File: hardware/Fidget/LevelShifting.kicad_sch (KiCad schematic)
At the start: 18 parts

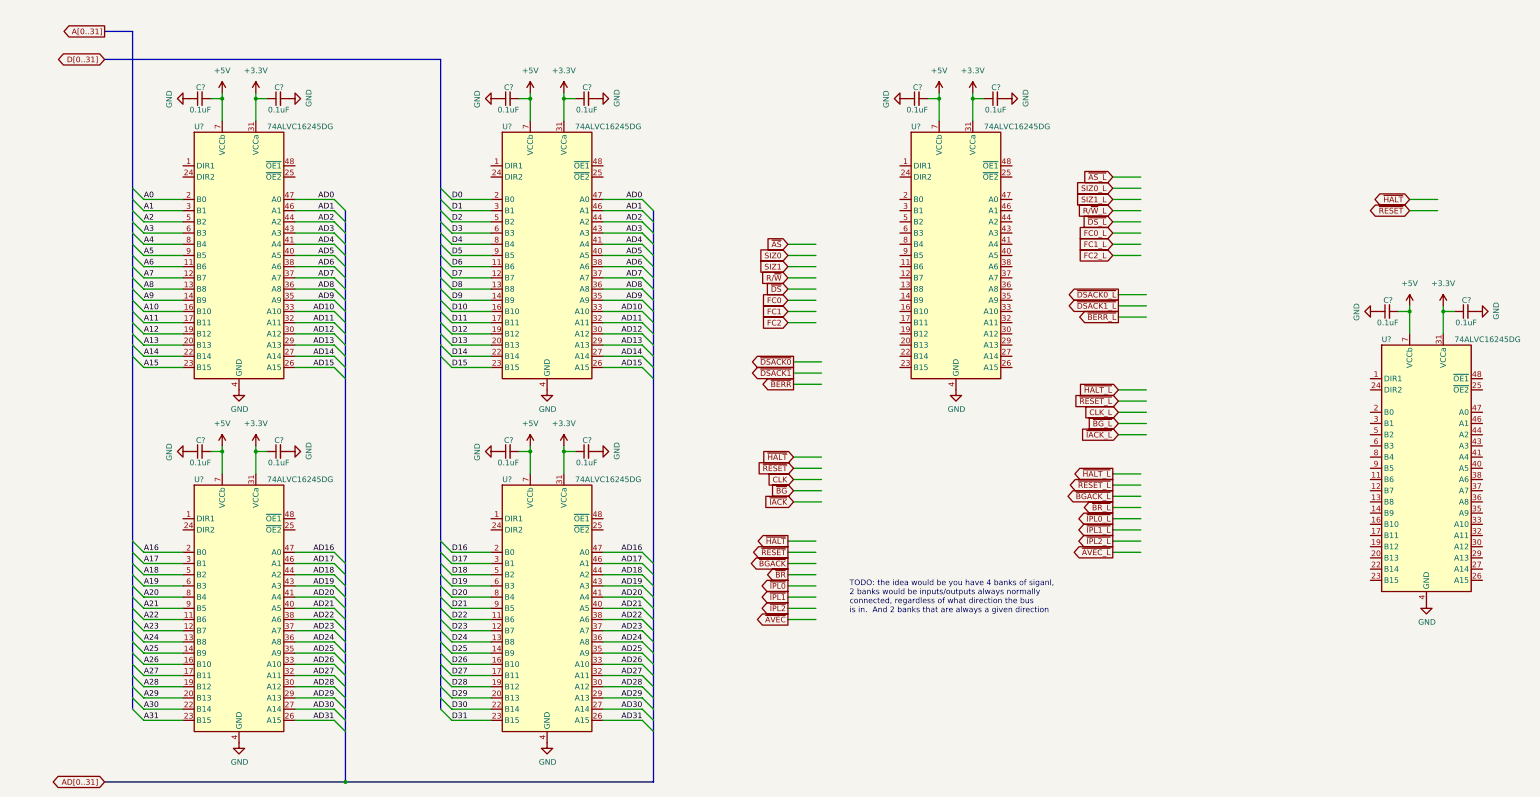
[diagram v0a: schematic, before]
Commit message: Assigned bus control signals to level shifters
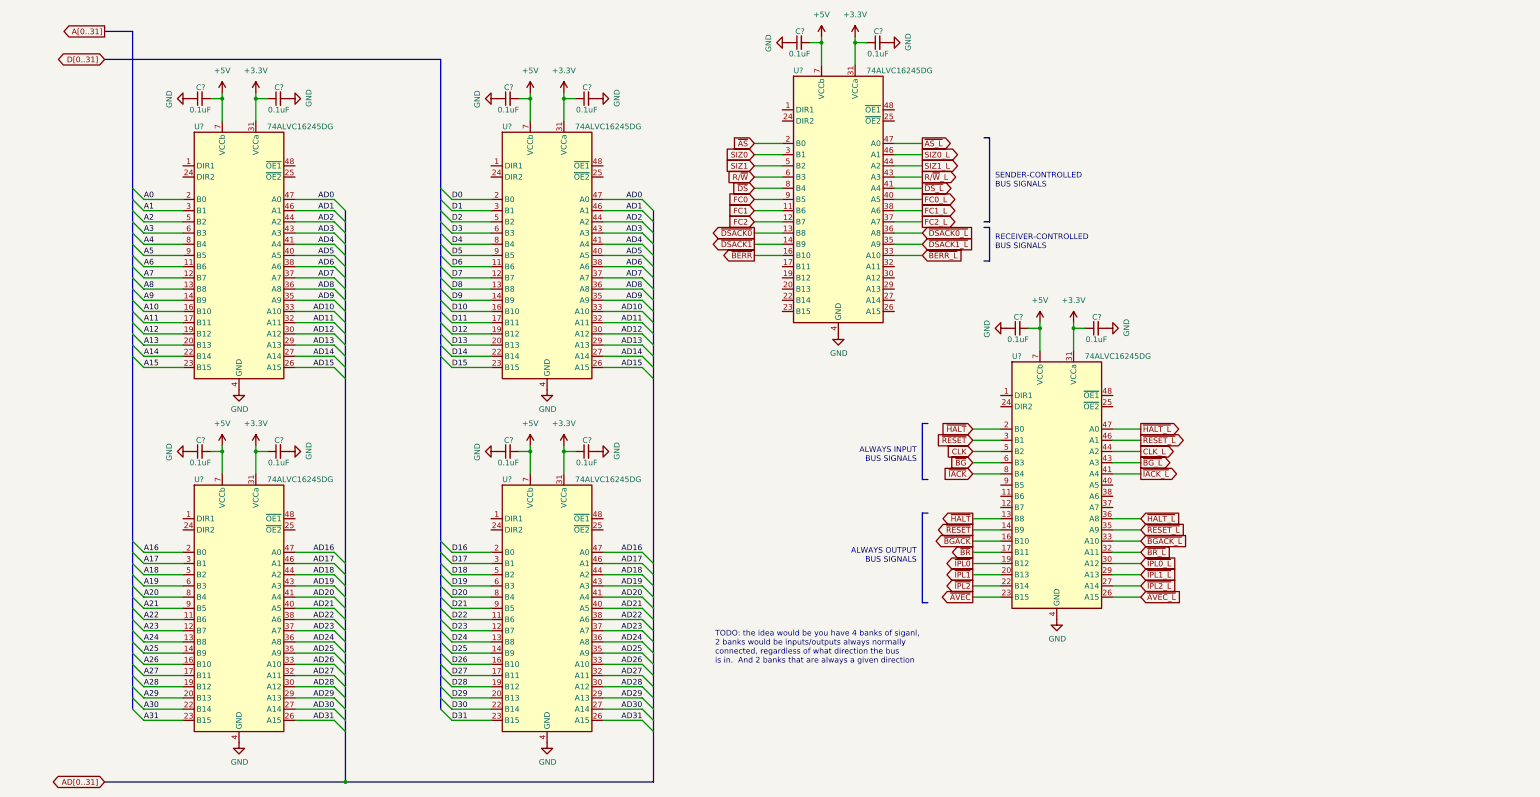
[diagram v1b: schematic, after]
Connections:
- net CLK: now also U?.5 (B2)
- net CLK_L: now also U?.44 (A2)
- net FC0: now also U?.9 (B5)
- net FC0_L: now also U?.40 (A5)
- net FC1: now also U?.11 (B6)
- net FC1_L: now also U?.38 (A6)
- net FC2: now also U?.12 (B7)
- net FC2_L: now also U?.37 (A7)
- net R/~{W}: now also U?.6 (B3)
- net R/~{W}_L: now also U?.43 (A3)
- net SIZ0: now also U?.3 (B1)
- net SIZ0_L: now also U?.46 (A1)
- net SIZ1: now also U?.5 (B2)
- net SIZ1_L: now also U?.44 (A2)
- net ~{AS_L}: now also U?.47 (A0)
- net ~{AS}: now also U?.2 (B0)
- net ~{AVEC_L}: now also U?.26 (A15)
- net ~{AVEC}: now also U?.23 (B15)
- net ~{BERR_L}: now also U?.33 (A10)
- net ~{BERR}: now also U?.16 (B10)
- net ~{BGACK_L}: now also U?.33 (A10)
- net ~{BGACK}: now also U?.16 (B10)
- net ~{BG_L}: now also U?.43 (A3)
- net ~{BG}: now also U?.6 (B3)
- net ~{BR_L}: now also U?.32 (A11)
- net ~{BR}: now also U?.17 (B11)
- net ~{DSACK0_L}: now also U?.36 (A8)
- net ~{DSACK0}: now also U?.13 (B8)
- net ~{DSACK1_L}: now also U?.35 (A9)
- net ~{DSACK1}: now also U?.14 (B9)
- net ~{DS_L}: now also U?.41 (A4)
- net ~{DS}: now also U?.8 (B4)
- net ~{HALT_L}: now also U?.36 (A8), U?.47 (A0)
- net ~{HALT}: now also U?.13 (B8), U?.2 (B0)
- net ~{IACK_L}: now also U?.41 (A4)
- net ~{IACK}: now also U?.8 (B4)
- net ~{IPL0_L}: now also U?.30 (A12)
- net ~{IPL0}: now also U?.19 (B12)
- net ~{IPL1_L}: now also U?.29 (A13)
- net ~{IPL1}: now also U?.20 (B13)
- net ~{IPL2_L}: now also U?.27 (A14)
- net ~{IPL2}: now also U?.22 (B14)
- net ~{RESET_L}: now also U?.35 (A9), U?.46 (A1)
- net ~{RESET}: now also U?.14 (B9), U?.3 (B1)
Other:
- note added: "ALWAYS INPUT BUS SIGNALS"
- note added: "ALWAYS OUTPUT BUS SIGNALS"
- note added: "RECEIVER-CONTROLLED BUS SIGNALS"
- note added: "SENDER-CONTROLLED BUS SIGNALS"
- moved on the sheet: C?, U?

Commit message: Added address latches
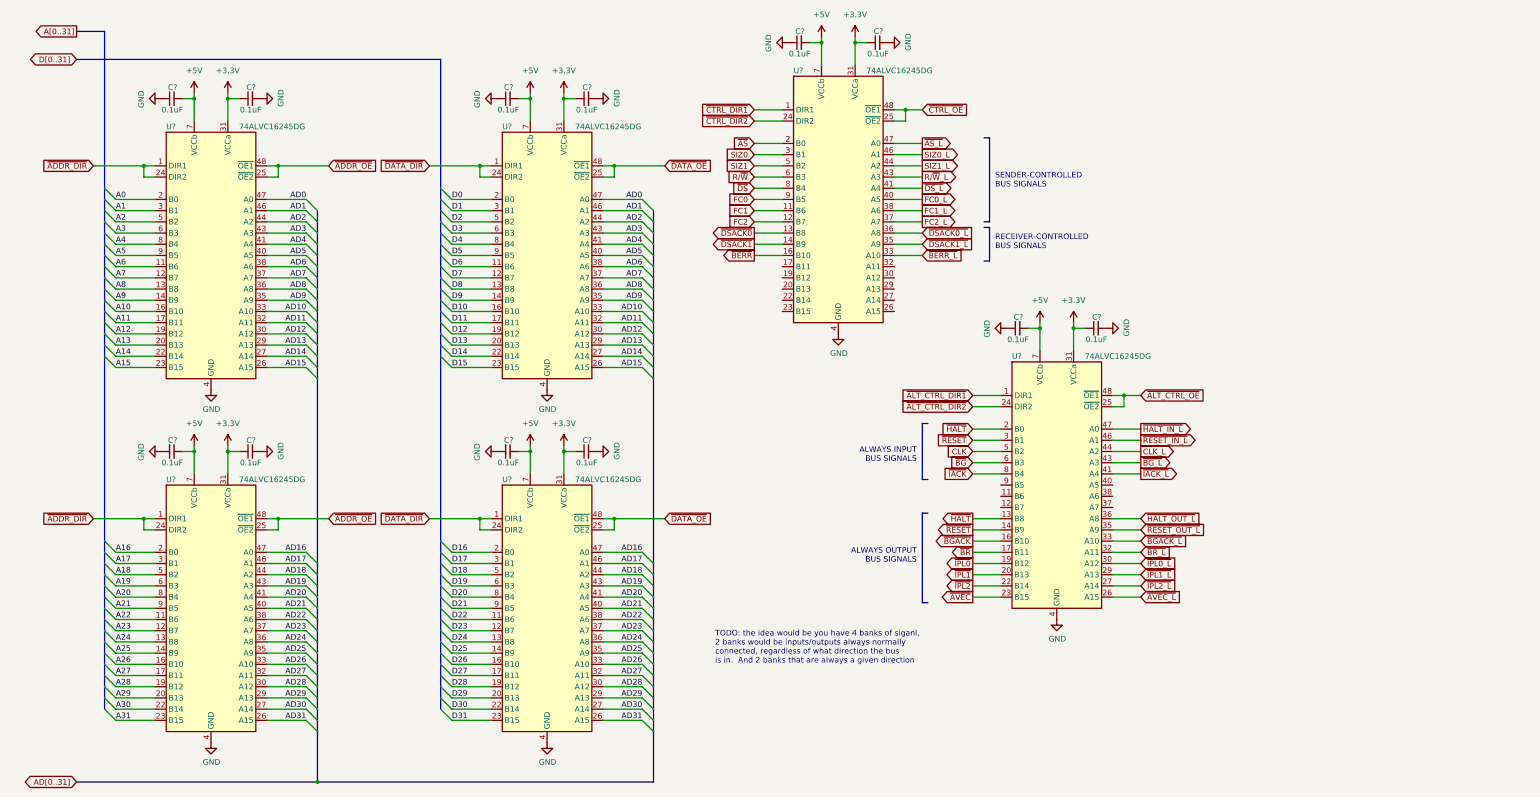
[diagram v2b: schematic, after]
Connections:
- net ~{DATA_DIR}: now reaches U?.1 (DIR1)
- net ~{DATA_DIR}: now also U?.1 (DIR1), U?.24 (DIR2), U?.24 (DIR2)
- net ~{DATA_OE}: now reaches U?.25 (~{OE2})
- net ~{DATA_OE}: now also U?.25 (~{OE2}), U?.48 (~{OE1}), U?.48 (~{OE1})
- net ~{ADDR_DIR}: now reaches U?.1 (DIR1)
- net ~{ADDR_DIR}: now also U?.1 (DIR1), U?.24 (DIR2), U?.24 (DIR2)
- net ~{ADDR_OE}: now reaches U?.25 (~{OE2})
- net ~{ADDR_OE}: now also U?.25 (~{OE2}), U?.48 (~{OE1}), U?.48 (~{OE1})
- net ~{CTRL_DIR1}: now reaches U?.1 (DIR1)
- net ~{CTRL_DIR2}: now reaches U?.24 (DIR2)
- net ~{CTRL_OE}: now reaches U?.25 (~{OE2})
- net ~{CTRL_OE}: now also U?.48 (~{OE1})
- net ~{ALT_CTRL_DIR1}: now reaches U?.1 (DIR1)
- net ~{ALT_CTRL_DIR2}: now reaches U?.24 (DIR2)
- net ~{ALT_CTRL_OE}: now reaches U?.25 (~{OE2})
- net ~{ALT_CTRL_OE}: now also U?.48 (~{OE1})
- net ~{HALT_L} renamed ~{HALT_IN_L}
- net ~{HALT_IN_L}: no longer U?.36 (A8)
- net ~{RESET_L} renamed ~{RESET_IN_L}
- net ~{RESET_IN_L}: no longer U?.35 (A9)
- new net ~{HALT_OUT_L}: U?.36 (A8)
- new net ~{RESET_OUT_L}: U?.35 (A9)
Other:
- moved on the sheet: C?, U?

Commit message: Progress on sorting out the transceiver controls
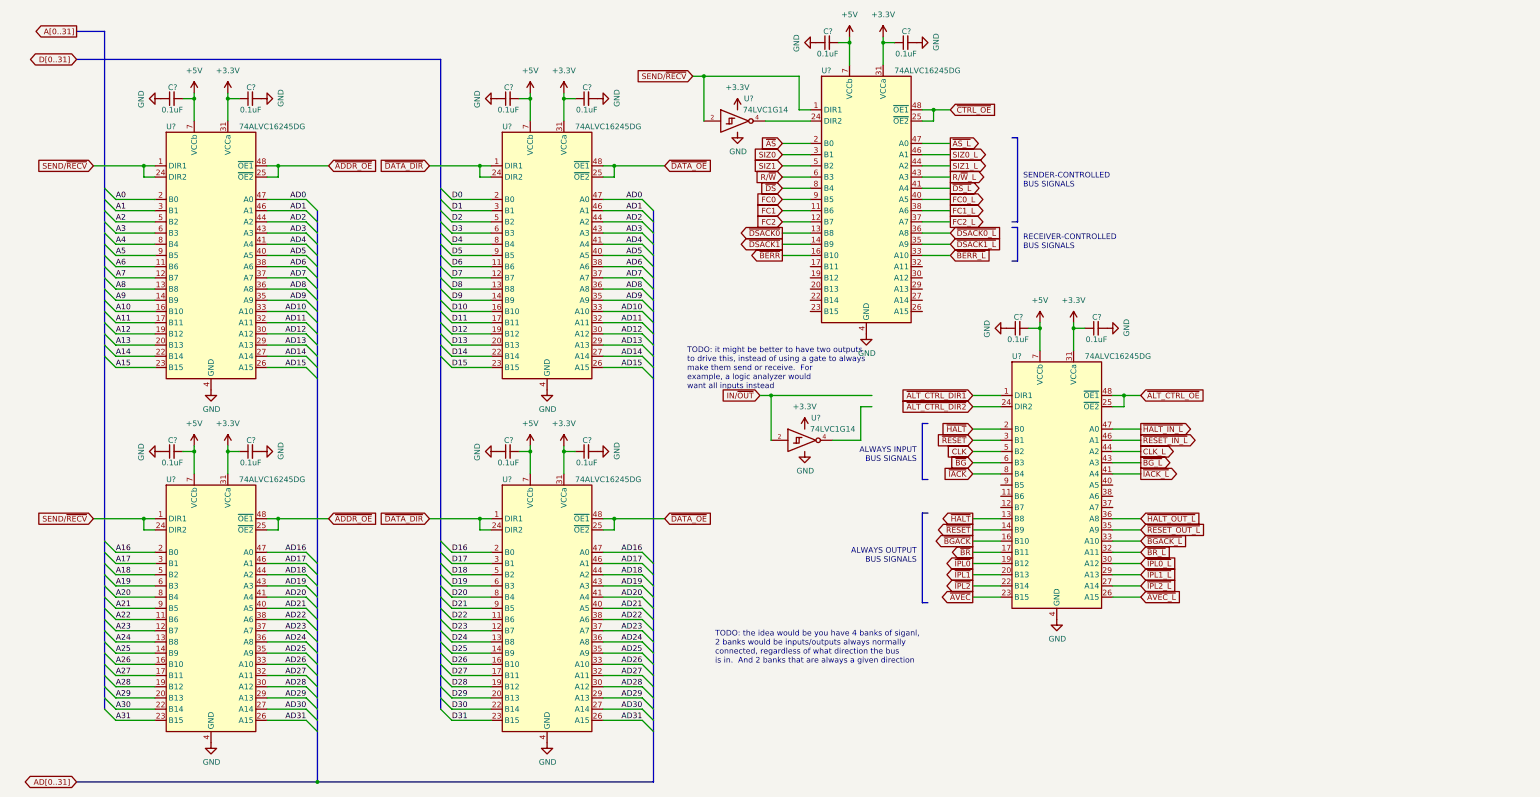
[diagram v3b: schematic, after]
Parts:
- added U? (x2): 74LVC1G14, symbol 74xGxx:74LVC1G14
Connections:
- net ~{CTRL_DIR1} is gone; now on net SEND/~{RECV}: U?.1 (DIR1)
- net +3.3V: now also U?.5 (VCC), U?.5 (VCC)
- net GND: now also U?.3 (GND), U?.3 (GND)
- net ~{ADDR_DIR} renamed SEND/~{RECV}
- net SEND/~{RECV}: now also U?.2
- net ~{CTRL_DIR2}: no longer names the net of U?.24 (DIR2)
- net ~{CTRL_DIR2}: now also U?.4
- new net IN/~{OUT}: U?.2
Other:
- note added: "TODO: it might be better to have two outputs to drive this, instead of using a gate to always make them send or receive. For example, a logic analyzer would want all inputs instead"
- moved on the sheet: C?, U?
